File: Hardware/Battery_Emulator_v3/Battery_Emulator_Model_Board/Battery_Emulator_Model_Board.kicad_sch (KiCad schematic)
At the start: 44 parts, among them J1 Vin, J10 Conn_01x05, J11 Conn_01x05, J12 Conn_01x05, J13 Conn_01x05, J14 Conn_01x05, J15 Conn_01x05, J16 Conn_01x05, J17 Conn_01x05, J2 USB4105-GF-A-060, J3 Conn_01x05, J5 Conn_01x05, J6 Conn_01x05, J7 Conn_01x05, J8 Conn_01x05, J9 Conn_01x05, U1 ATmega328PB-A, U2 KA78M05_TO252, U3 FT230XS-R, U4 74AHC2G125DP,125, Y1 Crystal_GND24

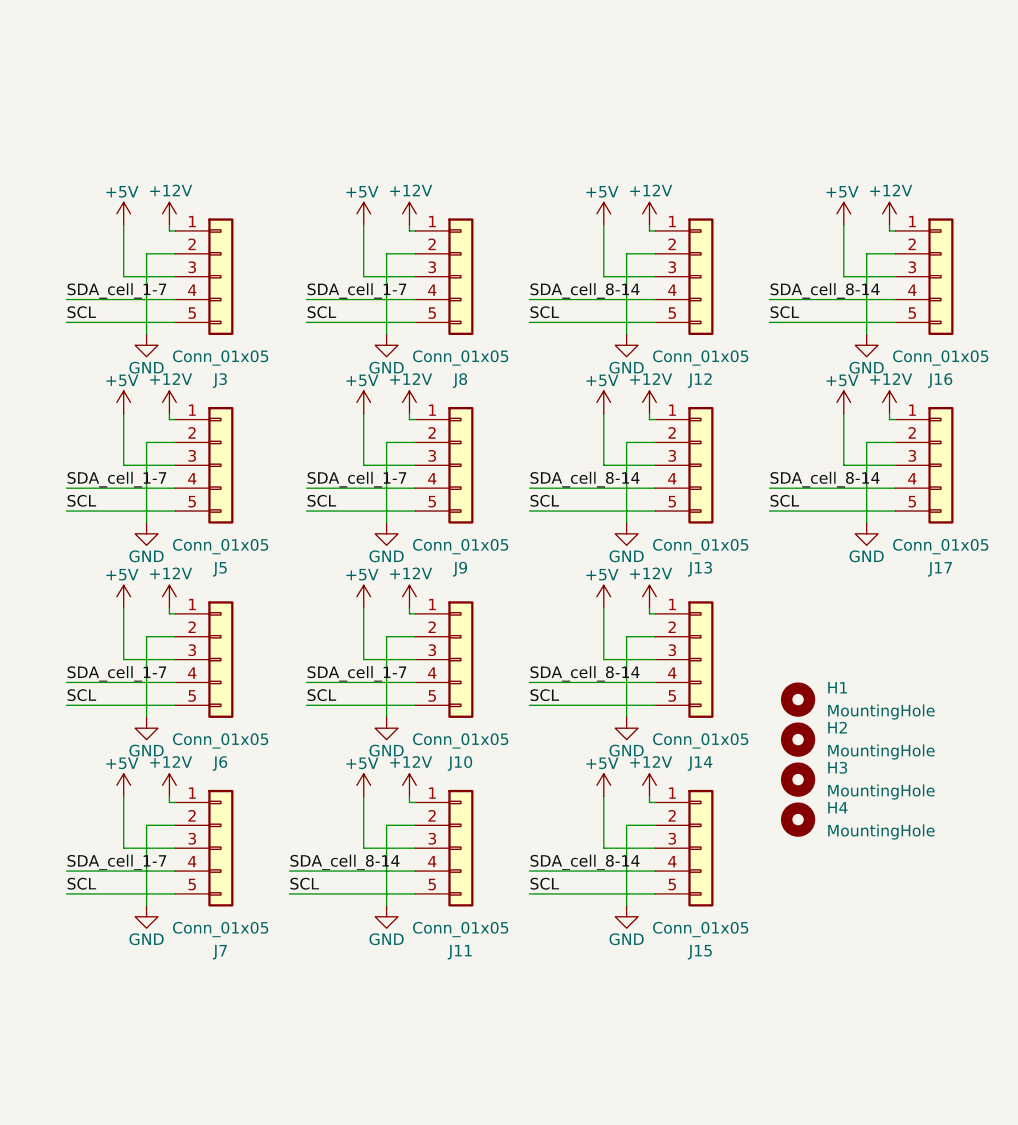
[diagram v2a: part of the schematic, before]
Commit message: Updated Mother board and Cell board
Changed pinout of mother board and cell board such that the pin headers are on the top side. Finished mother board PCB and did DRC check on it.
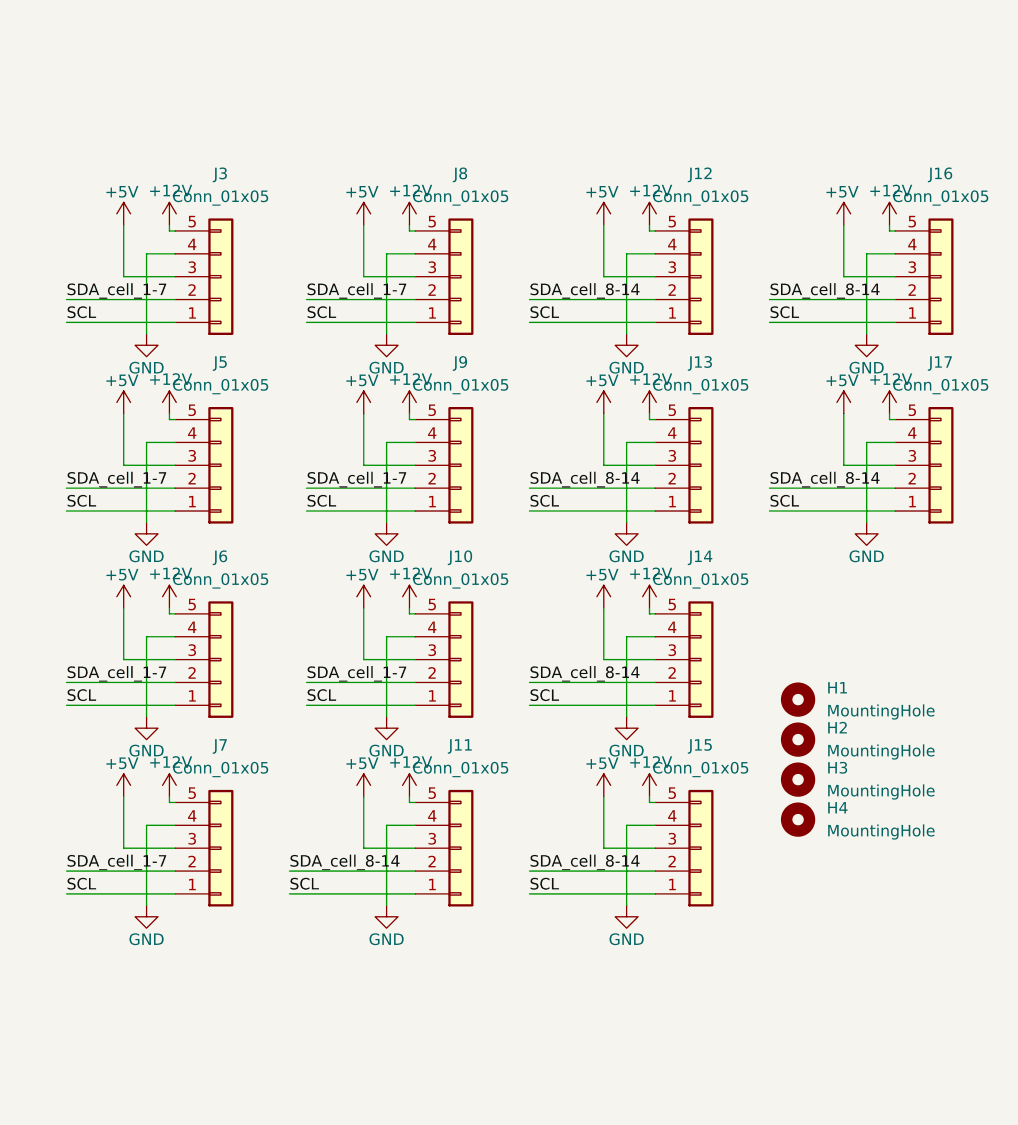
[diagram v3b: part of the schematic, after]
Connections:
- net +12V: now also J10.5 (Pin_5), J11.5 (Pin_5), J12.5 (Pin_5), J13.5 (Pin_5), J14.5 (Pin_5), J15.5 (Pin_5), J16.5 (Pin_5), J17.5 (Pin_5), J3.5 (Pin_5), J5.5 (Pin_5), J6.5 (Pin_5), J7.5 (Pin_5), J8.5 (Pin_5), J9.5 (Pin_5); no longer J10.1 (Pin_1), J11.1 (Pin_1), J12.1 (Pin_1), J13.1 (Pin_1), J14.1 (Pin_1), J15.1 (Pin_1), J16.1 (Pin_1), J17.1 (Pin_1), J3.1 (Pin_1), J5.1 (Pin_1), J6.1 (Pin_1), J7.1 (Pin_1), J8.1 (Pin_1), J9.1 (Pin_1)
- net GND: now also J10.4 (Pin_4), J11.4 (Pin_4), J12.4 (Pin_4), J13.4 (Pin_4), J14.4 (Pin_4), J15.4 (Pin_4), J16.4 (Pin_4), J17.4 (Pin_4), J3.4 (Pin_4), J5.4 (Pin_4), J6.4 (Pin_4), J7.4 (Pin_4), J8.4 (Pin_4), J9.4 (Pin_4); no longer J10.2 (Pin_2), J11.2 (Pin_2), J12.2 (Pin_2), J13.2 (Pin_2), J14.2 (Pin_2), J15.2 (Pin_2), J16.2 (Pin_2), J17.2 (Pin_2), J3.2 (Pin_2), J5.2 (Pin_2), J6.2 (Pin_2), J7.2 (Pin_2), J8.2 (Pin_2), J9.2 (Pin_2)
- net SCL: now also J10.1 (Pin_1), J11.1 (Pin_1), J12.1 (Pin_1), J13.1 (Pin_1), J14.1 (Pin_1), J15.1 (Pin_1), J16.1 (Pin_1), J17.1 (Pin_1), J3.1 (Pin_1), J5.1 (Pin_1), J6.1 (Pin_1), J7.1 (Pin_1), J8.1 (Pin_1), J9.1 (Pin_1); no longer J10.5 (Pin_5), J11.5 (Pin_5), J12.5 (Pin_5), J13.5 (Pin_5), J14.5 (Pin_5), J15.5 (Pin_5), J16.5 (Pin_5), J17.5 (Pin_5), J3.5 (Pin_5), J5.5 (Pin_5), J6.5 (Pin_5), J7.5 (Pin_5), J8.5 (Pin_5), J9.5 (Pin_5)
- net SDA_cell_1-7: now also J10.2 (Pin_2), J3.2 (Pin_2), J5.2 (Pin_2), J6.2 (Pin_2), J7.2 (Pin_2), J8.2 (Pin_2), J9.2 (Pin_2); no longer J10.4 (Pin_4), J3.4 (Pin_4), J5.4 (Pin_4), J6.4 (Pin_4), J7.4 (Pin_4), J8.4 (Pin_4), J9.4 (Pin_4)
- net SDA_cell_8-14: now also J11.2 (Pin_2), J12.2 (Pin_2), J13.2 (Pin_2), J14.2 (Pin_2), J15.2 (Pin_2), J16.2 (Pin_2), J17.2 (Pin_2); no longer J11.4 (Pin_4), J12.4 (Pin_4), J13.4 (Pin_4), J14.4 (Pin_4), J15.4 (Pin_4), J16.4 (Pin_4), J17.4 (Pin_4)
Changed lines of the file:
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@@
     (effects (font (size 1.27 1.27)) (justify left bottom))
   )
-  (symbol (lib_id "Connector_Generic:Conn_01x05") (at 195.58 99.695 0) (unit 1)
-    (in_bom yes) (on_board yes) (dnp no)
-    (property "Reference" "J5" (at 195.58 111.125 0)
-      (effects (font (size 1.27 1.27)))
-    )
-    (property "Value" "Conn_01x05" (at 195.58 108.585 0)
+  (symbol (lib_id "Connector_Generic:Conn_01x05") (at 195.58 99.695 0) (mirror x) (unit 1)
+    (in_bom yes) (on_board yes) (dnp no)
+    (property "Reference" "J5" (at 195.58 88.265 0)
+      (effects (font (size 1.27 1.27)))
+    )
+    (property "Value" "Conn_01x05" (at 195.58 90.805 0)
       (effects (font (size 1.27 1.27)))
     )
@@
     )
   )
-  (symbol (lib_id "Connector_Generic:Conn_01x05") (at 275.59 99.695 0) (unit 1)
-    (in_bom yes) (on_board yes) (dnp no)
-    (property "Reference" "J17" (at 275.59 111.125 0)
-      (effects (font (size 1.27 1.27)))
-    )
-    (property "Value" "Conn_01x05" (at 275.59 108.585 0)
+  (symbol (lib_id "Connector_Generic:Conn_01x05") (at 275.59 99.695 0) (mirror x) (unit 1)
+    (in_bom yes) (on_board yes) (dnp no)
+    (property "Reference" "J17" (at 275.59 88.265 0)
+      (effects (font (size 1.27 1.27)))
+    )
+    (property "Value" "Conn_01x05" (at 275.59 90.805 0)
       (effects (font (size 1.27 1.27)))
     )
@@
     )
   )
-  (symbol (lib_id "Connector_Generic:Conn_01x05") (at 248.92 142.24 0) (unit 1)
-    (in_bom yes) (on_board yes) (dnp no)
-    (property "Reference" "J15" (at 248.92 153.67 0)
-      (effects (font (size 1.27 1.27)))
-    )
-    (property "Value" "Conn_01x05" (at 248.92 151.13 0)
+  (symbol (lib_id "Connector_Generic:Conn_01x05") (at 248.92 142.24 0) (mirror x) (unit 1)
+    (in_bom yes) (on_board yes) (dnp no)
+    (property "Reference" "J15" (at 248.92 130.81 0)
+      (effects (font (size 1.27 1.27)))
+    )
+    (property "Value" "Conn_01x05" (at 248.92 133.35 0)
       (effects (font (size 1.27 1.27)))
     )
@@
     )
   )
-  (symbol (lib_id "Connector_Generic:Conn_01x05") (at 248.92 78.74 0) (unit 1)
-    (in_bom yes) (on_board yes) (dnp no)
-    (property "Reference" "J12" (at 248.92 90.17 0)
-      (effects (font (size 1.27 1.27)))
-    )
-    (property "Value" "Conn_01x05" (at 248.92 87.63 0)
+  (symbol (lib_id "Connector_Generic:Conn_01x05") (at 248.92 78.74 0) (mirror x) (unit 1)
+    (in_bom yes) (on_board yes) (dnp no)
+    (property "Reference" "J12" (at 248.92 67.31 0)
+      (effects (font (size 1.27 1.27)))
+    )
+    (property "Value" "Conn_01x05" (at 248.92 69.85 0)
       (effects (font (size 1.27 1.27)))
     )
@@
     )
   )
-  (symbol (lib_id "Connector_Generic:Conn_01x05") (at 195.58 121.285 0) (unit 1)
-    (in_bom yes) (on_board yes) (dnp no)
-    (property "Reference" "J6" (at 195.58 132.715 0)
-      (effects (font (size 1.27 1.27)))
-    )
-    (property "Value" "Conn_01x05" (at 195.58 130.175 0)
+  (symbol (lib_id "Connector_Generic:Conn_01x05") (at 195.58 121.285 0) (mirror x) (unit 1)
+    (in_bom yes) (on_board yes) (dnp no)
+    (property "Reference" "J6" (at 195.58 109.855 0)
+      (effects (font (size 1.27 1.27)))
+    )
+    (property "Value" "Conn_01x05" (at 195.58 112.395 0)
       (effects (font (size 1.27 1.27)))
     )
@@
     )
   )
-  (symbol (lib_id "Connector_Generic:Conn_01x05") (at 222.25 99.695 0) (unit 1)
-    (in_bom yes) (on_board yes) (dnp no)
-    (property "Reference" "J9" (at 222.25 111.125 0)
-      (effects (font (size 1.27 1.27)))
-    )
-    (property "Value" "Conn_01x05" (at 222.25 108.585 0)
+  (symbol (lib_id "Connector_Generic:Conn_01x05") (at 222.25 99.695 0) (mirror x) (unit 1)
+    (in_bom yes) (on_board yes) (dnp no)
+    (property "Reference" "J9" (at 222.25 88.265 0)
+      (effects (font (size 1.27 1.27)))
+    )
+    (property "Value" "Conn_01x05" (at 222.25 90.805 0)
       (effects (font (size 1.27 1.27)))
     )
@@
     )
   )
-  (symbol (lib_id "Connector_Generic:Conn_01x05") (at 248.92 99.695 0) (unit 1)
-    (in_bom yes) (on_board yes) (dnp no)
-    (property "Reference" "J13" (at 248.92 111.125 0)
-      (effects (font (size 1.27 1.27)))
-    )
-    (property "Value" "Conn_01x05" (at 248.92 108.585 0)
+  (symbol (lib_id "Connector_Generic:Conn_01x05") (at 248.92 99.695 0) (mirror x) (unit 1)
+    (in_bom yes) (on_board yes) (dnp no)
+    (property "Reference" "J13" (at 248.92 88.265 0)
+      (effects (font (size 1.27 1.27)))
+    )
+    (property "Value" "Conn_01x05" (at 248.92 90.805 0)
       (effects (font (size 1.27 1.27)))
     )
@@
     )
   )
-  (symbol (lib_id "Connector_Generic:Conn_01x05") (at 195.58 78.74 0) (unit 1)
-    (in_bom yes) (on_board yes) (dnp no)
-    (property "Reference" "J3" (at 195.58 90.17 0)
-      (effects (font (size 1.27 1.27)))
-    )
-    (property "Value" "Conn_01x05" (at 195.58 87.63 0)
+  (symbol (lib_id "Connector_Generic:Conn_01x05") (at 195.58 78.74 0) (mirror x) (unit 1)
+    (in_bom yes) (on_board yes) (dnp no)
+    (property "Reference" "J3" (at 195.58 67.31 0)
+      (effects (font (size 1.27 1.27)))
+    )
+    (property "Value" "Conn_01x05" (at 195.58 69.85 0)
       (effects (font (size 1.27 1.27)))
     )
@@
     )
   )
-  (symbol (lib_id "Connector_Generic:Conn_01x05") (at 222.25 121.285 0) (unit 1)
-    (in_bom yes) (on_board yes) (dnp no)
-    (property "Reference" "J10" (at 222.25 132.715 0)
-      (effects (font (size 1.27 1.27)))
-    )
-    (property "Value" "Conn_01x05" (at 222.25 130.175 0)
+  (symbol (lib_id "Connector_Generic:Conn_01x05") (at 222.25 121.285 0) (mirror x) (unit 1)
+    (in_bom yes) (on_board yes) (dnp no)
+    (property "Reference" "J10" (at 222.25 109.855 0)
+      (effects (font (size 1.27 1.27)))
+    )
+    (property "Value" "Conn_01x05" (at 222.25 112.395 0)
       (effects (font (size 1.27 1.27)))
     )
@@
     )
   )
-  (symbol (lib_id "Connector_Generic:Conn_01x05") (at 222.25 78.74 0) (unit 1)
-    (in_bom yes) (on_board yes) (dnp no)
-    (property "Reference" "J8" (at 222.25 90.17 0)
-      (effects (font (size 1.27 1.27)))
-    )
-    (property "Value" "Conn_01x05" (at 222.25 87.63 0)
+  (symbol (lib_id "Connector_Generic:Conn_01x05") (at 222.25 78.74 0) (mirror x) (unit 1)
+    (in_bom yes) (on_board yes) (dnp no)
+    (property "Reference" "J8" (at 222.25 67.31 0)
+      (effects (font (size 1.27 1.27)))
+    )
+    (property "Value" "Conn_01x05" (at 222.25 69.85 0)
       (effects (font (size 1.27 1.27)))
     )
@@
     )
   )
-  (symbol (lib_id "Connector_Generic:Conn_01x05") (at 275.59 78.74 0) (unit 1)
-    (in_bom yes) (on_board yes) (dnp no)
-    (property "Reference" "J16" (at 275.59 90.17 0)
-      (effects (font (size 1.27 1.27)))
-    )
-    (property "Value" "Conn_01x05" (at 275.59 87.63 0)
+  (symbol (lib_id "Connector_Generic:Conn_01x05") (at 275.59 78.74 0) (mirror x) (unit 1)
+    (in_bom yes) (on_board yes) (dnp no)
+    (property "Reference" "J16" (at 275.59 67.31 0)
+      (effects (font (size 1.27 1.27)))
+    )
+    (property "Value" "Conn_01x05" (at 275.59 69.85 0)
       (effects (font (size 1.27 1.27)))
     )
@@
     )
   )
-  (symbol (lib_id "Connector_Generic:Conn_01x05") (at 222.25 142.24 0) (unit 1)
-    (in_bom yes) (on_board yes) (dnp no)
-    (property "Reference" "J11" (at 222.25 153.67 0)
-      (effects (font (size 1.27 1.27)))
-    )
-    (property "Value" "Conn_01x05" (at 222.25 151.13 0)
+  (symbol (lib_id "Connector_Generic:Conn_01x05") (at 222.25 142.24 0) (mirror x) (unit 1)
+    (in_bom yes) (on_board yes) (dnp no)
+    (property "Reference" "J11" (at 222.25 130.81 0)
+      (effects (font (size 1.27 1.27)))
+    )
+    (property "Value" "Conn_01x05" (at 222.25 133.35 0)
       (effects (font (size 1.27 1.27)))
     )
@@
     )
   )
-  (symbol (lib_id "Connector_Generic:Conn_01x05") (at 195.58 142.24 0) (unit 1)
-    (in_bom yes) (on_board yes) (dnp no)
-    (property "Reference" "J7" (at 195.58 153.67 0)
-      (effects (font (size 1.27 1.27)))
-    )
-    (property "Value" "Conn_01x05" (at 195.58 151.13 0)
+  (symbol (lib_id "Connector_Generic:Conn_01x05") (at 195.58 142.24 0) (mirror x) (unit 1)
+    (in_bom yes) (on_board yes) (dnp no)
+    (property "Reference" "J7" (at 195.58 130.81 0)
+      (effects (font (size 1.27 1.27)))
+    )
+    (property "Value" "Conn_01x05" (at 195.58 133.35 0)
       (effects (font (size 1.27 1.27)))
     )
@@
     )
   )
-  (symbol (lib_id "Connector_Generic:Conn_01x05") (at 248.92 121.285 0) (unit 1)
-    (in_bom yes) (on_board yes) (dnp no)
-    (property "Reference" "J14" (at 248.92 132.715 0)
-      (effects (font (size 1.27 1.27)))
-    )
-    (property "Value" "Conn_01x05" (at 248.92 130.175 0)
-      (effects (font (size 1.27 1.27)))
-    )
+  (symbol (lib_id "Connector_Generic:Conn_01x05") (at 248.92 121.285 0) (mirror x) (unit 1)
+    (in_bom yes) (on_board yes) (dnp no)
+    (property "Reference" "J14" (at 248.92 109.855 0)
+      (effects (font (size 1.27 1.27)))
+    )
+    (property "Value" "Conn_01x05" (at 248.92 112.395 0)
+      (effects (font (size 1.27 1.27)))
+    )

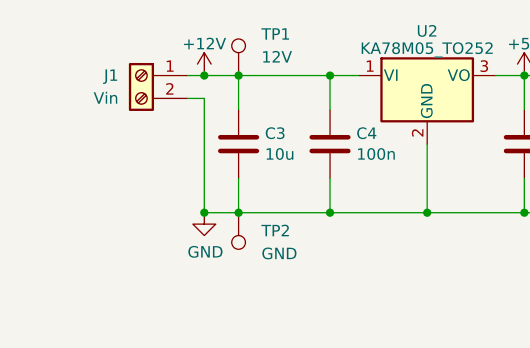
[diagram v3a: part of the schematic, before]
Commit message: added reverse polarity protection
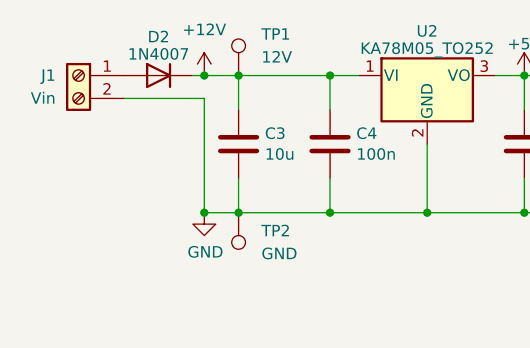
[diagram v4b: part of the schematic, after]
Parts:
- added D2: 1N4007, Diode_THT:D_DO-41_SOD81_P10.16mm_Horizontal, symbol Diode:1N4007
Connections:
- net +12V: now also D2.1 (K); no longer J1.1 (Pin_1)
- new net: D2.2 (A), J1.1 (Pin_1)
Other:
- moved on the sheet: J1
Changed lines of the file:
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@@
+    (stroke (width 0) (type default))
+  )
+  (wire (pts (xy 34.29 21.59) (xy 35.56 21.59))
     (stroke (width 0) (type default))
   )
@@
     (stroke (width 0) (type default))
   )
-  (wire (pts (xy 33.655 21.59) (xy 35.56 21.59))
-    (stroke (width 0) (type default))
-  )
   (wire (pts (xy 90.17 137.16) (xy 93.345 137.16))
     (stroke (width 0) (type default))
@@
     (stroke (width 0) (type default))
   )
-  (wire (pts (xy 33.655 24.13) (xy 35.56 24.13))
+  (wire (pts (xy 26.67 24.13) (xy 35.56 24.13))
     (stroke (width 0) (type default))
   )
@@
     )
   )
+  (symbol (lib_id "Diode:1N4007") (at 30.48 21.59 0) (mirror y) (unit 1)
+    (in_bom yes) (on_board yes) (dnp no) (fields_autoplaced)
+    (property "Reference" "D2" (at 30.48 17.3101 0)
+      (effects (font (size 1.27 1.27)))
+    )
+    (property "Value" "1N4007" (at 30.48 19.2311 0)
+      (effects (font (size 1.27 1.27)))
+    )
+    (property "Footprint" "Diode_THT:D_DO-41_SOD81_P10.16mm_Horizontal" (at 30.48 26.035 0)
+      (effects (font (size 1.27 1.27)) hide)
+    )
+    (property "Datasheet" "http://www.vishay.com/docs/88503/1n4001.pdf" (at 30.48 21.59 0)
+      (effects (font (size 1.27 1.27)) hide)
+    )
+    (property "Sim.Device" "D" (at 30.48 21.59 0)
+      (effects (font (size 1.27 1.27)) hide)
+    )
+    (property "Sim.Pins" "1=K 2=A" (at 30.48 21.59 0)
+      (effects (font (size 1.27 1.27)) hide)
+    )
+    (pin "1")
+    (pin "2")
+    (instances
+      (project "Battery_Emulator_Model_Board"
+        (path "/148b0eed-bd25-41de-bd25-36484a90c6fc"
+          (reference "D2") (unit 1)
+        )
+      )
+    )
+  )
   (symbol (lib_id "PR7 Custom:74AHC2G125DP,125") (at 107.315 29.21 0) (unit 3)
     (in_bom yes) (on_board yes) (dnp no)
@@
   )
   (symbol (lib_id "power:+12V") (at 35.56 21.59 0) (unit 1)
-    (in_bom yes) (on_board yes) (dnp no) (fields_autoplaced)
+    (in_bom yes) (on_board yes) (dnp no)
     (property "Reference" "#PWR04" (at 35.56 25.4 0)
       (effects (font (size 1.27 1.27)) hide)
     )
-    (property "Value" "+12V" (at 35.56 18.0881 0)
+    (property "Value" "+12V" (at 35.56 16.51 0)
       (effects (font (size 1.27 1.27)))
     )
@@
     )
   )
-  (symbol (lib_id "Connector:Screw_Terminal_01x02") (at 28.575 21.59 0) (mirror y) (unit 1)
-    (in_bom yes) (on_board yes) (dnp no)
-    (property "Reference" "J1" (at 26.035 21.59 0)
-      (effects (font (size 1.27 1.27)) (justify left))
-    )
-    (property "Value" "Vin" (at 26.035 24.13 0)
-      (effects (font (size 1.27 1.27)) (justify left))
-    )
-    (property "Footprint" "TerminalBlock_Phoenix:TerminalBlock_Phoenix_MKDS-1,5-2-5.08_1x02_P5.08mm_Horizontal" (at 28.575 21.59 0)
-      (effects (font (size 1.27 1.27)) hide)
-    )
-    (property "Datasheet" "~" (at 28.575 21.59 0)
-      (effects (font (size 1.27 1.27)) hide)
-    )
+  (symbol (lib_id "Connector:Screw_Terminal_01x02") (at 21.59 21.59 0) (mirror y) (unit 1)
+    (in_bom yes) (on_board yes) (dnp no)
+    (property "Reference" "J1" (at 19.05 21.59 0)
+      (effects (font (size 1.27 1.27)) (justify left))
+    )
+    (property "Value" "Vin" (at 19.05 24.13 0)
+      (effects (font (size 1.27 1.27)) (justify left))
+    )
+    (property "Footprint" "TerminalBlock_Phoenix:TerminalBlock_Phoenix_MKDS-1,5-2-5.08_1x02_P5.08mm_Horizontal" (at 21.59 21.59 0)
+      (effects (font (size 1.27 1.27)) hide)
+    )
+    (property "Datasheet" "~" (at 21.59 21.59 0)
+      (effects (font (size 1.27 1.27)) hide)
+    )

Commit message: added diode
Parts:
- added H5, H6, H7, H8: MountingHole, MountingHole:MountingHole_3.2mm_M3_Pad_Via, symbol Mechanical:MountingHole_Pad
- D2: footprint Diode_THT:D_DO-41_SOD81_P10.16mm_Horizontal -> Diode_THT:D_DO-41_SOD81_P2.54mm_Vertical_KathodeUp
- H1, H2, H3, H4: footprint MountingHole:MountingHole_3.2mm_M3 -> MountingHole:MountingHole_3.2mm_M3_Pad_Via; symbol Mechanical:MountingHole -> Mechanical:MountingHole_Pad
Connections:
- net GND: now also H1.1, H2.1, H3.1, H4.1, H5.1, H6.1, H7.1, H8.1
